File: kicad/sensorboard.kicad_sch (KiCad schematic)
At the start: 2 parts, among them U3 TMP117MAIDRVT, U5 SHT40-AD1B-R2

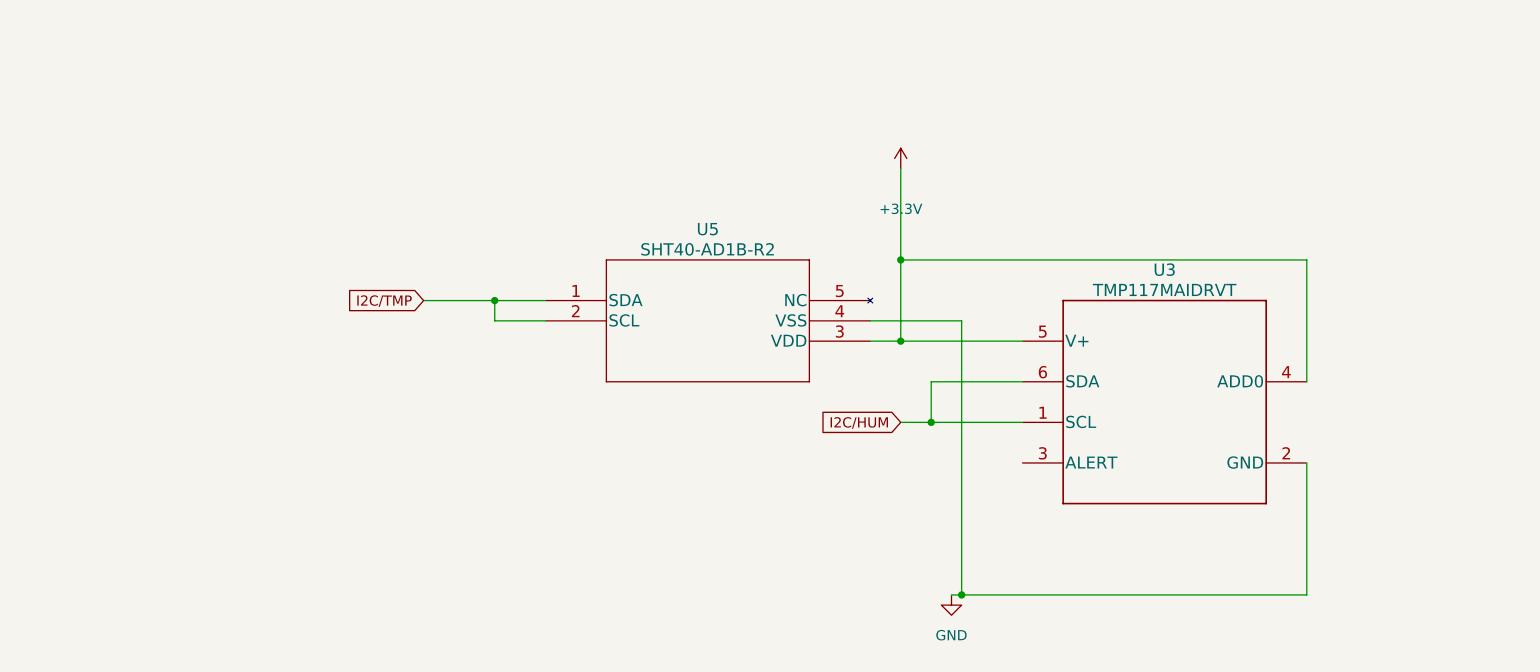
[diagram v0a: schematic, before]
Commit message: sensorboard schema + esd datasheet
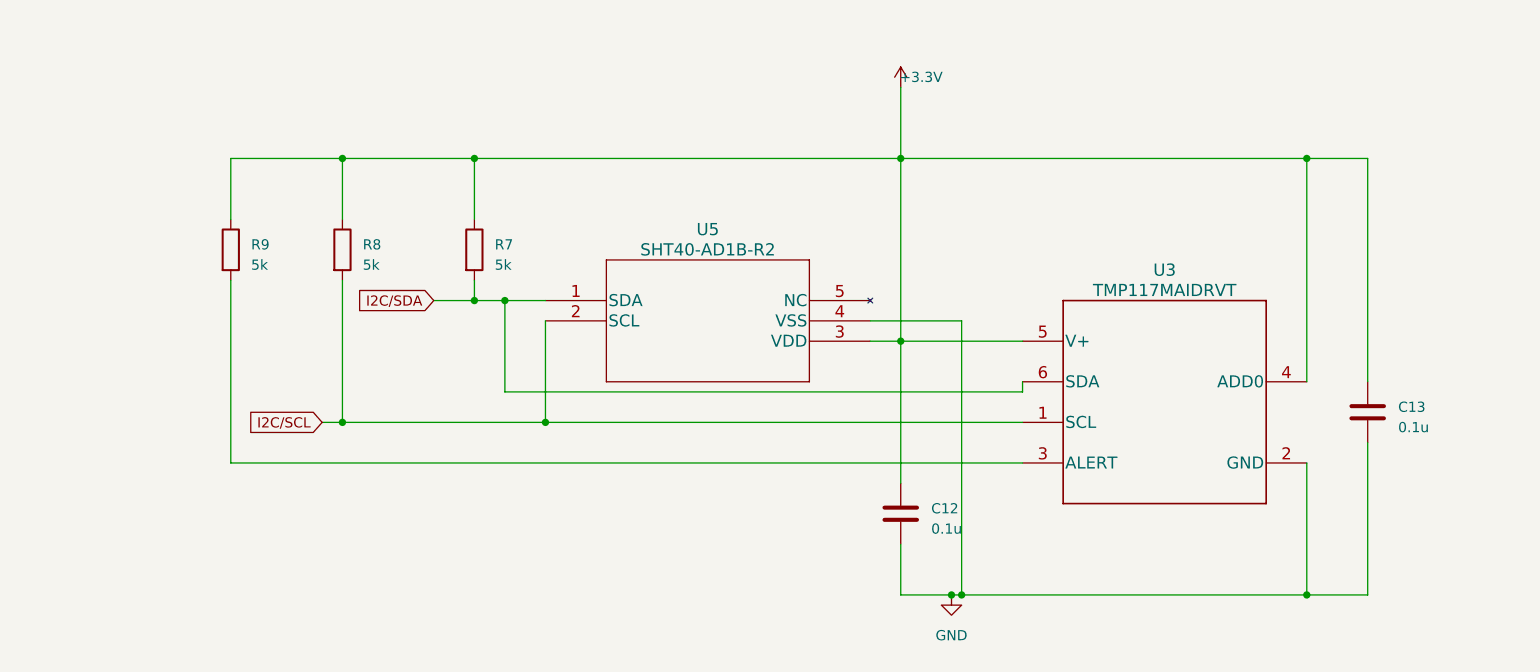
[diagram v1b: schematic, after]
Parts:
- added C12, C13: 0.1u, symbol Device:C
- added R7, R8, R9: 5k, symbol Device:R
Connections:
- net +3.3V: now also C12.1, C13.1, R7.1, R8.1, R9.1
- net GND: now also C12.2, C13.2
- net at U3.3 (ALERT): now also R9.2
- net I2C/HUM renamed I2C/SCL
- net I2C/SCL: now also U5.2 (SCL), R8.2; no longer U3.6 (SDA)
- net I2C/TMP renamed I2C/SDA
- net I2C/SDA: now also U3.6 (SDA), R7.2; no longer U5.2 (SCL)

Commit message: added comments and muokkasin komponenttiennumeroinnin selvemmäksi.
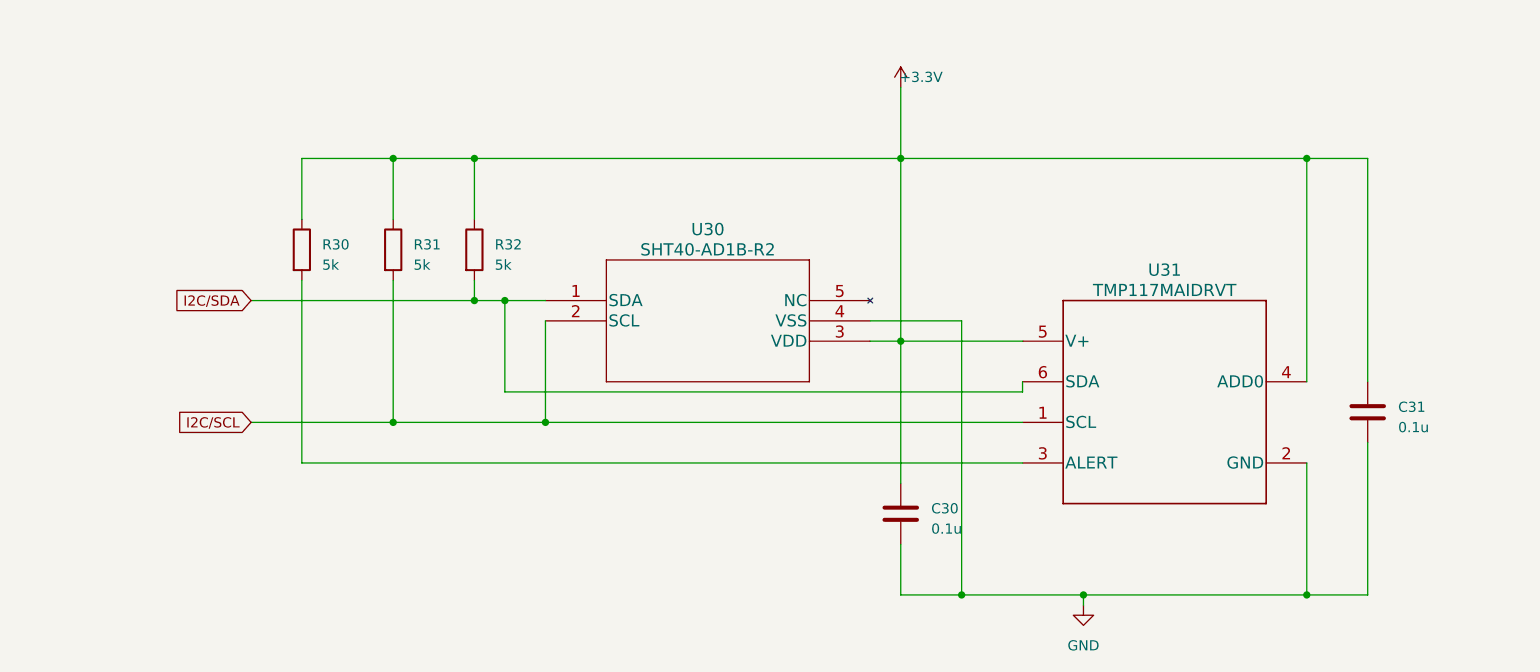
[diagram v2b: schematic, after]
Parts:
- renumbered C12 to C30, C13 to C31, R9 to R30, R8 to R31, R7 to R32, U5 to U30, U3 to U31
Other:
- moved on the sheet: R30, R31

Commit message: Added Digikey part number and footprint to symbols, added signal TMP_ALERT
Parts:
- U30: footprint SHT4x_SEN -> SHT-40AD1B-R2:SHT40-AD1B-R2; Digikey (none) -> 1649-SHT40-AD1B-R3CT-ND
- U31: footprint DRV0006B -> TMP117MAIDRVT:TMP117MAIDRVT; Digikey (none) -> 296-52215-1-ND
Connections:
- net TMP_ALERT: now reaches R30.2, U31.3 (ALERT)
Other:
- title: (none) -> External boar for temperature and humidity sensors
- moved on the sheet: C30, C31, R30, R31, R32, U30, U31

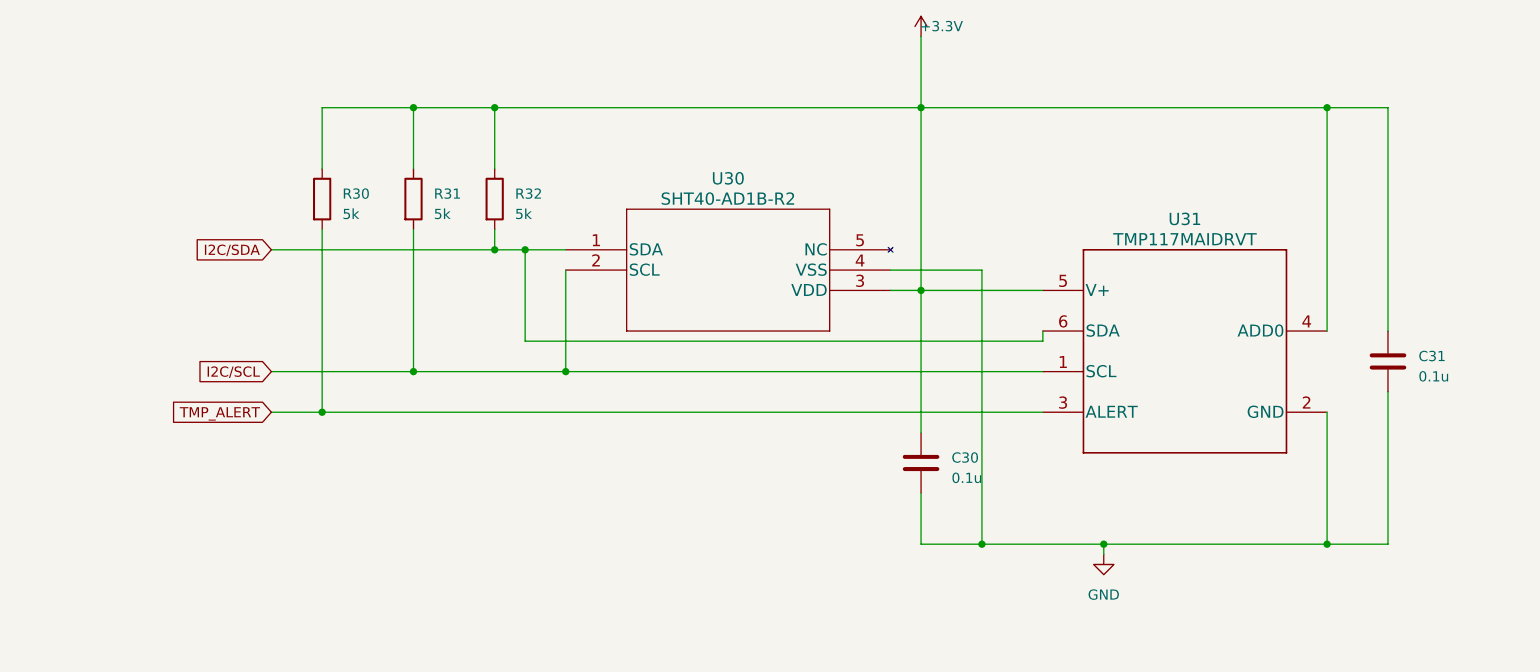
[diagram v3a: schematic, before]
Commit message: Added buttons and connectors
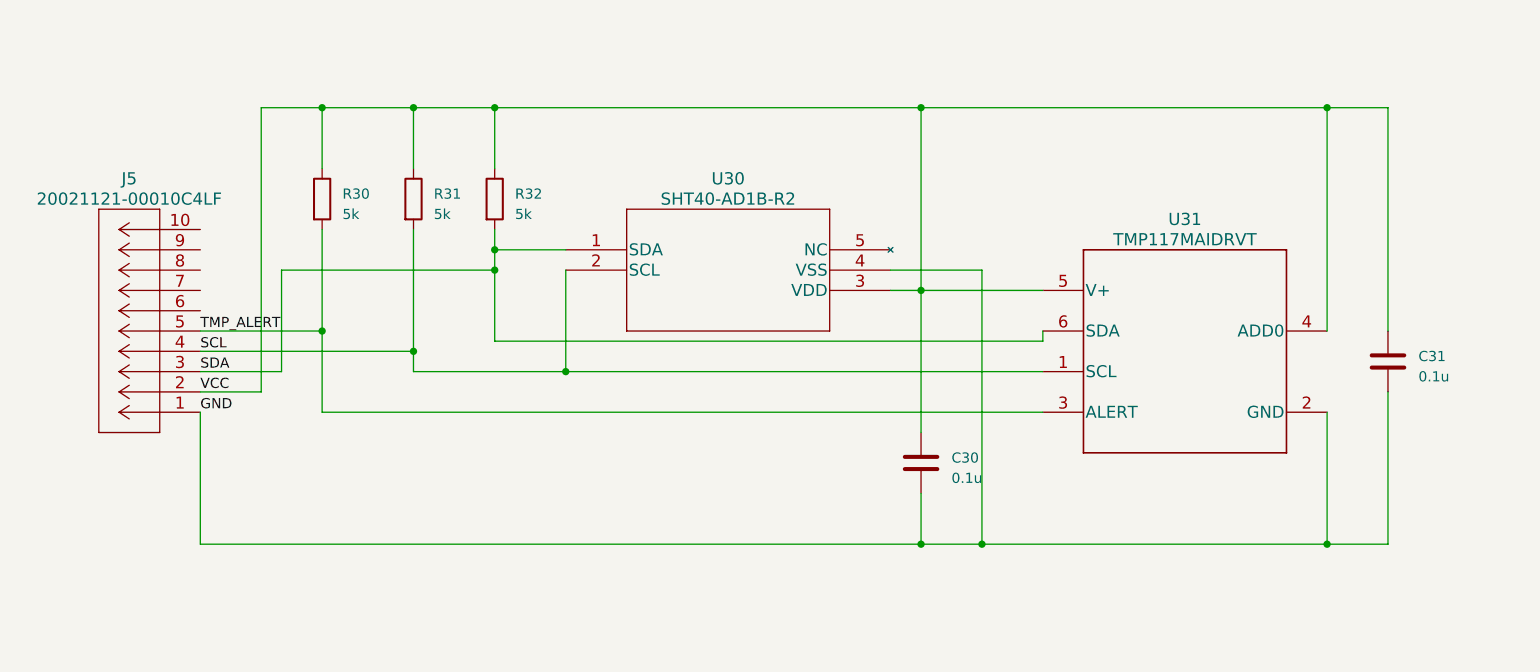
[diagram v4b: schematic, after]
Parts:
- added J5: 20021121-00010C4LF, CONN_00010C4LF_AMP, symbol 20021121-00010C4LF:20021121-00010C4LF
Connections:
- net GND: now also J5.1
- net TMP_ALERT: now also J5.5
- net +3.3V renamed VCC
- net VCC: now also J5.2
- net I2C/SCL renamed SCL
- net SCL: now also J5.4
- net I2C/SDA renamed SDA
- net SDA: now also J5.3
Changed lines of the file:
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@@
   (junction (at 118.11 31.75) (diameter 0) (color 0 0 0 0)
   )
-  (junction (at 43.18 69.85) (diameter 0) (color 0 0 0 0)
-  )
-  (junction (at 68.58 49.53) (diameter 0) (color 0 0 0 0)
+  (junction (at 43.18 31.75) (diameter 0) (color 0 0 0 0)
+  )
+  (junction (at 43.18 59.69) (diameter 0) (color 0 0 0 0)
+  )
+  (junction (at 54.61 31.75) (diameter 0) (color 0 0 0 0)
   )
   (junction (at 64.77 49.53) (diameter 0) (color 0 0 0 0)
   )
-  (junction (at 54.61 31.75) (diameter 0) (color 0 0 0 0)
-  )
-  (junction (at 140.97 86.36) (diameter 0) (color 0 0 0 0)
-  )
   (junction (at 125.73 86.36) (diameter 0) (color 0 0 0 0)
   )
   (junction (at 168.91 31.75) (diameter 0) (color 0 0 0 0)
   )
+  (junction (at 118.11 86.36) (diameter 0) (color 0 0 0 0)
+  )
   (junction (at 118.11 54.61) (diameter 0) (color 0 0 0 0)
   )
   (junction (at 64.77 31.75) (diameter 0) (color 0 0 0 0)
   )
-  (junction (at 54.61 64.77) (diameter 0) (color 0 0 0 0)
+  (junction (at 64.77 52.07) (diameter 0) (color 0 0 0 0)
   )
   (junction (at 73.66 64.77) (diameter 0) (color 0 0 0 0)
@@
   (junction (at 168.91 86.36) (diameter 0) (color 0 0 0 0)
   )
+  (junction (at 54.61 62.23) (diameter 0) (color 0 0 0 0)
+  )
   (wire (pts (xy 118.11 54.61) (xy 118.11 72.39))
     (stroke (width 0) (type default))
   )
-  (wire (pts (xy 140.97 86.36) (xy 140.97 87.63))
-    (stroke (width 0) (type default))
-  )
   (wire (pts (xy 54.61 64.77) (xy 73.66 64.77))
     (stroke (width 0) (type default))
   )
+  (wire (pts (xy 27.94 62.23) (xy 54.61 62.23))
+    (stroke (width 0) (type default))
+  )
   (wire (pts (xy 43.18 31.75) (xy 54.61 31.75))
     (stroke (width 0) (type default))
@@
     (stroke (width 0) (type default))
   )
-  (wire (pts (xy 125.73 86.36) (xy 140.97 86.36))
+  (wire (pts (xy 35.56 67.31) (xy 35.56 31.75))
+    (stroke (width 0) (type default))
+  )
+  (wire (pts (xy 125.73 86.36) (xy 168.91 86.36))
+    (stroke (width 0) (type default))
+  )
+  (wire (pts (xy 27.94 59.69) (xy 43.18 59.69))
     (stroke (width 0) (type default))
   )
@@
     (stroke (width 0) (type default))
   )
+  (wire (pts (xy 64.77 60.96) (xy 64.77 52.07))
+    (stroke (width 0) (type default))
+  )
+  (wire (pts (xy 64.77 52.07) (xy 64.77 49.53))
+    (stroke (width 0) (type default))
+  )
+  (wire (pts (xy 38.1 64.77) (xy 38.1 52.07))
+    (stroke (width 0) (type default))
+  )
+  (wire (pts (xy 43.18 59.69) (xy 43.18 69.85))
+    (stroke (width 0) (type default))
+  )
   (wire (pts (xy 125.73 52.07) (xy 125.73 86.36))
     (stroke (width 0) (type default))
   )
-  (wire (pts (xy 68.58 49.53) (xy 73.66 49.53))
-    (stroke (width 0) (type default))
-  )
-  (wire (pts (xy 36.83 69.85) (xy 43.18 69.85))
+  (wire (pts (xy 64.77 49.53) (xy 73.66 49.53))
     (stroke (width 0) (type default))
   )
@@
     (stroke (width 0) (type default))
   )
-  (wire (pts (xy 118.11 22.86) (xy 118.11 31.75))
-    (stroke (width 0) (type default))
-  )
   (wire (pts (xy 64.77 46.99) (xy 64.77 49.53))
     (stroke (width 0) (type default))
@@
     (stroke (width 0) (type default))
   )
-  (wire (pts (xy 140.97 86.36) (xy 168.91 86.36))
+  (wire (pts (xy 38.1 52.07) (xy 64.77 52.07))
     (stroke (width 0) (type default))
   )
@@
     (stroke (width 0) (type default))
   )
-  (wire (pts (xy 54.61 46.99) (xy 54.61 64.77))
-    (stroke (width 0) (type default))
-  )
-  (wire (pts (xy 64.77 49.53) (xy 68.58 49.53))
-    (stroke (width 0) (type default))
-  )
-  (wire (pts (xy 43.18 46.99) (xy 43.18 69.85))
-    (stroke (width 0) (type default))
-  )
-  (wire (pts (xy 36.83 64.77) (xy 54.61 64.77))
+  (wire (pts (xy 54.61 46.99) (xy 54.61 62.23))
+    (stroke (width 0) (type default))
+  )
+  (wire (pts (xy 43.18 31.75) (xy 35.56 31.75))
+    (stroke (width 0) (type default))
+  )
+  (wire (pts (xy 43.18 46.99) (xy 43.18 59.69))
     (stroke (width 0) (type default))
   )
@@
     (stroke (width 0) (type default))
   )
+  (wire (pts (xy 54.61 62.23) (xy 54.61 64.77))
+    (stroke (width 0) (type default))
+  )
   (wire (pts (xy 73.66 52.07) (xy 73.66 64.77))
     (stroke (width 0) (type default))
   )
-  (wire (pts (xy 36.83 49.53) (xy 64.77 49.53))
-    (stroke (width 0) (type default))
-  )
   (wire (pts (xy 54.61 31.75) (xy 64.77 31.75))
     (stroke (width 0) (type default))
@@
     (stroke (width 0) (type default))
   )
+  (wire (pts (xy 27.94 67.31) (xy 35.56 67.31))
+    (stroke (width 0) (type default))
+  )
   (wire (pts (xy 114.3 54.61) (xy 118.11 54.61))
     (stroke (width 0) (type default))
@@
     (stroke (width 0) (type default))
   )
-  (wire (pts (xy 68.58 60.96) (xy 133.35 60.96))
+  (wire (pts (xy 27.94 69.85) (xy 27.94 86.36))
+    (stroke (width 0) (type default))
+  )
+  (wire (pts (xy 64.77 60.96) (xy 133.35 60.96))
     (stroke (width 0) (type default))
   )
@@
     (stroke (width 0) (type default))
   )
+  (wire (pts (xy 27.94 86.36) (xy 118.11 86.36))
+    (stroke (width 0) (type default))
+  )
   (wire (pts (xy 168.91 69.85) (xy 168.91 86.36))
     (stroke (width 0) (type default))
   )
-  (wire (pts (xy 68.58 49.53) (xy 68.58 60.96))
-    (stroke (width 0) (type default))
-  )
-  (global_label "TMP_ALERT" (shape input) (at 36.83 69.85 180) (fields_autoplaced)
-    (effects (font (size 1.27 1.27)) (justify right))
-    (property "Intersheetrefs" "${INTERSHEET_REFS}" (at 23.7643 69.85 0)
-      (effects (font (size 1.27 1.27)) (justify right) hide)
-    )
-  )
-  (global_label "I2C{slash}SDA" (shape input) (at 36.83 49.53 180) (fields_autoplaced)
-    (effects (font (size 1.27 1.27)) (justify right))
-    (property "Intersheetrefs" "${INTERSHEET_REFS}" (at 25.9413 49.53 0)
-      (effects (font (size 1.27 1.27)) (justify right) hide)
-    )
-  )
-  (global_label "I2C{slash}SCL" (shape input) (at 36.83 64.77 180) (fields_autoplaced)
-    (effects (font (size 1.27 1.27)) (justify right))
-    (property "Intersheetrefs" "${INTERSHEET_REFS}" (at 26.0018 64.77 0)
-      (effects (font (size 1.27 1.27)) (justify right) hide)
-    )
+  (wire (pts (xy 27.94 64.77) (xy 38.1 64.77))
+    (stroke (width 0) (type default))
+  )
+  (label "TMP_ALERT" (at 27.94 59.69 0) (fields_autoplaced)
+    (effects (font (size 1.27 1.27)) (justify left bottom))
+  )
+  (label "VCC" (at 27.94 67.31 0) (fields_autoplaced)
+    (effects (font (size 1.27 1.27)) (justify left bottom))
+  )
+  (label "SCL" (at 27.94 62.23 0) (fields_autoplaced)
+    (effects (font (size 1.27 1.27)) (justify left bottom))
+  )
+  (label "SDA" (at 27.94 64.77 0) (fields_autoplaced)
+    (effects (font (size 1.27 1.27)) (justify left bottom))
+  )
+  (label "GND" (at 27.94 69.85 0) (fields_autoplaced)
+    (effects (font (size 1.27 1.27)) (justify left bottom))
   )
   (symbol (lib_id "Device:R") (at 43.18 43.18 0) (unit 1)
@@
         (path "/184b47ed-2c2b-4c02-be35-d18f4f4e5685/ce4dfdb9-1dc9-45f7-82b8-487b1ef6453b"
           (reference "C30") (unit 1)
-        )
-      )
-    )
-  )
-  (symbol (lib_id "power:GND") (at 140.97 87.63 0) (unit 1)
-    (in_bom yes) (on_board yes) (dnp no) (fields_autoplaced)
-    (property "Reference" "#PWR02" (at 140.97 93.98 0)
-      (effects (font (size 1.27 1.27)) hide)
-    )
-    (property "Value" "GND" (at 140.97 92.71 0)
-      (effects (font (size 1.27 1.27)))
-    )
-    (property "Footprint" "" (at 140.97 87.63 0)
-      (effects (font (size 1.27 1.27)) hide)
-    )
-    (property "Datasheet" "" (at 140.97 87.63 0)
-      (effects (font (size 1.27 1.27)) hide)
-    )
-    (pin "1")
-    (instances
-      (project "IoT_sulari"
-        (path "/184b47ed-2c2b-4c02-be35-d18f4f4e5685/900a775e-83e7-4530-ab2f-7e5f26c05ece"
-          (reference "#PWR02") (unit 1)
-        )
-        (path "/184b47ed-2c2b-4c02-be35-d18f4f4e5685/ce4dfdb9-1dc9-45f7-82b8-487b1ef6453b"
-          (reference "#PWR019") (unit 1)
         )
       )
@@
     )
   )
-  (symbol (lib_id "power:+3.3V") (at 118.11 22.86 0) (unit 1)
-    (in_bom yes) (on_board yes) (dnp no)
-    (property "Reference" "#PWR011" (at 118.11 26.67 0)
-      (effects (font (size 1.27 1.27)) hide)
-    )
-    (property "Value" "+3.3V" (at 120.65 21.59 0)
-      (effects (font (size 1.27 1.27)))
-    )
-    (property "Footprint" "" (at 118.11 22.86 0)
-      (effects (font (size 1.27 1.27)) hide)
-    )
-    (property "Datasheet" "" (at 118.11 22.86 0)
-      (effects (font (size 1.27 1.27)) hide)
-    )
-    (pin "1")
-    (instances
-      (project "IoT_sulari"
-        (path "/184b47ed-2c2b-4c02-be35-d18f4f4e5685"
-          (reference "#PWR011") (unit 1)
-        )
-        (path "/184b47ed-2c2b-4c02-be35-d18f4f4e5685/ce4dfdb9-1dc9-45f7-82b8-487b1ef6453b"
-          (reference "#PWR018") (unit 1)
-        )
-      )
-    )
-  )
   (symbol (lib_id "Device:R") (at 54.61 43.18 0) (unit 1)
     (in_bom yes) (on_board yes) (dnp no) (fields_autoplaced)
@@
         )
       )
+    )
+  )
+  (symbol (lib_id "20021121-00010C4LF:20021121-00010C4LF") (at 27.94 69.85 180) (unit 1)
+    (in_bom yes) (on_board yes) (dnp no) (fields_autoplaced)
+    (property "Reference" "J5" (at 19.05 40.64 0)
+      (effects (font (size 1.524 1.524)))
+    )
+    (property "Value" "20021121-00010C4LF" (at 19.05 43.18 0)
+      (effects (font (size 1.524 1.524)))
+    )
+    (property "Footprint" "CONN_00010C4LF_AMP" (at 17.78 58.166 0)
+      (effects (font (size 1.524 1.524)) hide)
+    )
+    (property "Datasheet" "" (at 27.94 69.85 0)
+      (effects (font (size 1.524 1.524)))
+    )
+    (pin "1")
+    (pin "10")
+    (pin "2")
+    (pin "3")
+    (pin "4")
+    (pin "5")
+    (pin "6")
+    (pin "7")
+    (pin "8")
+    (pin "9")
+    (instances
+      (project "IoT_sulari"
+        (path "/184b47ed-2c2b-4c02-be35-d18f4f4e5685/ce4dfdb9-1dc9-45f7-82b8-487b1ef6453b"
+          (reference "J5") (unit 1)
+        )
+      )
